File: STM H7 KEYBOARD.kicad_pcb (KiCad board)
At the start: 4 copper layers, 316.7 x 127 mm, 354 parts, among them J1 USB_C_Receptacle_USB2.0_16P, SW1 SW_Push, SW10 SW_Push, SW11 SW_Push, SW12 SW_Push, SW13 SW_Push, SW14 SW_Push, SW15 SW_Push, SW16 SW_Push, SW17 SW_Push, SW18 SW_Push, SW19 SW_Push, SW2 SW_Push, SW20 SW_Push, SW21 SW_Push, SW22 SW_Push, SW23 SW_Push, SW24 SW_Push, SW25 SW_Push, SW26 SW_Push, SW27 SW_Push, SW28 SW_Push, SW29 SW_Push, SW3 SW_Push, SW30 SW_Push, SW31 SW_Push, SW32 SW_Push, SW33 SW_Push, SW34 SW_Push, SW35 SW_Push, SW36 SW_Push, SW37 SW_Push, SW38 SW_Push, SW39 SW_Push, SW4 SW_Push, SW40 SW_Push, SW41 SW_Push, SW42 SW_Push, SW43 SW_Push, SW44 SW_Push, SW45 SW_Push, SW46 SW_Push, SW47 SW_Push, SW48 SW_Push, SW49 SW_Push, SW5 SW_Push, SW50 SW_Push, SW51 SW_Push, SW52 SW_Push, SW53 SW_Push, SW54 SW_Push, SW55 SW_Push, SW56 SW_Push, SW57 SW_Push, SW58 SW_Push, SW59 SW_Push, SW6 SW_Push, SW60 SW_Push, SW61 SW_Push, SW62 SW_Push, SW63 SW_Push, SW64 SW_Push, SW65 SW_Push, SW66 SW_Push, SW67 SW_Push, SW68 SW_Push, SW7 SW_Push, SW8 SW_Push, SW9 SW_Push, U1 USBLC6-2SC6, U2 AP63203WU, U4 STM32H723VGTx, U5 SN74AHCT1G125DBVR, U6 TPS25940LRVCR, U7 TUSB320LAIRWBR, Y1 8MHz

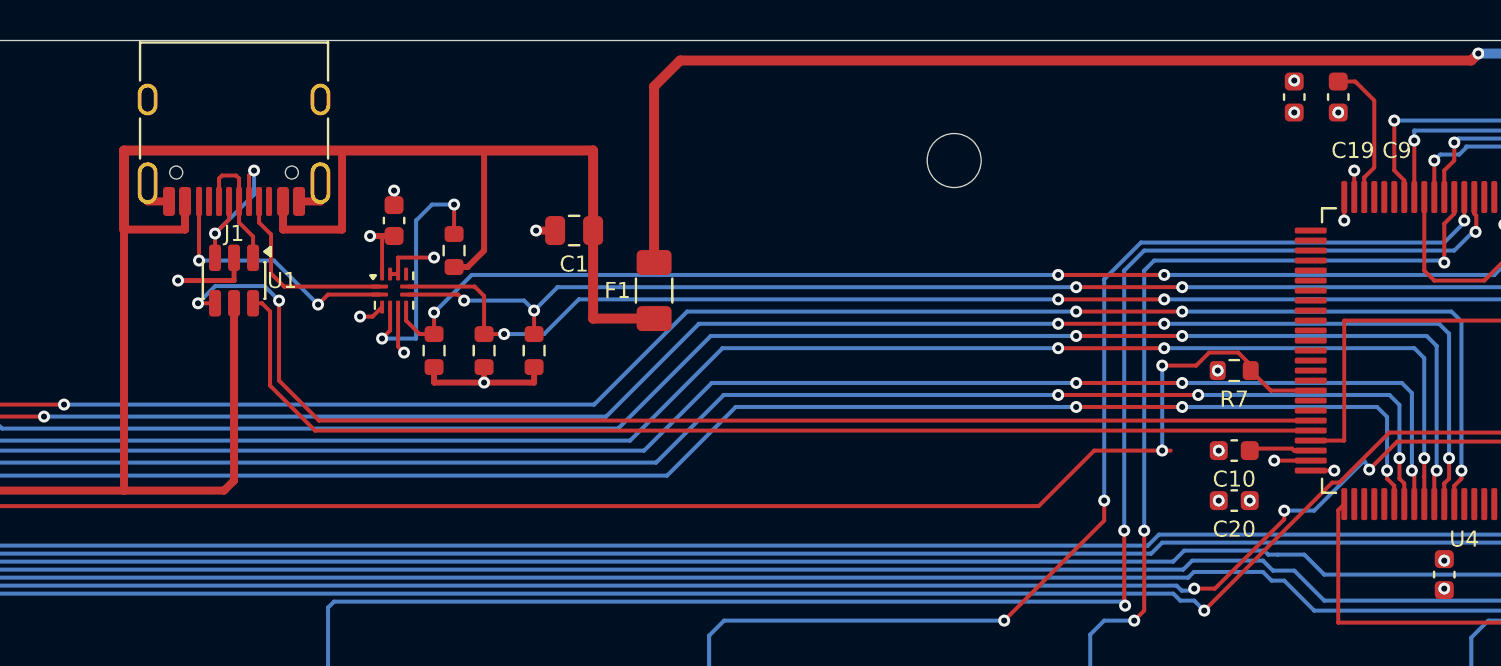
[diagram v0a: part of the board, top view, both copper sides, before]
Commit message: Fixed usb routing
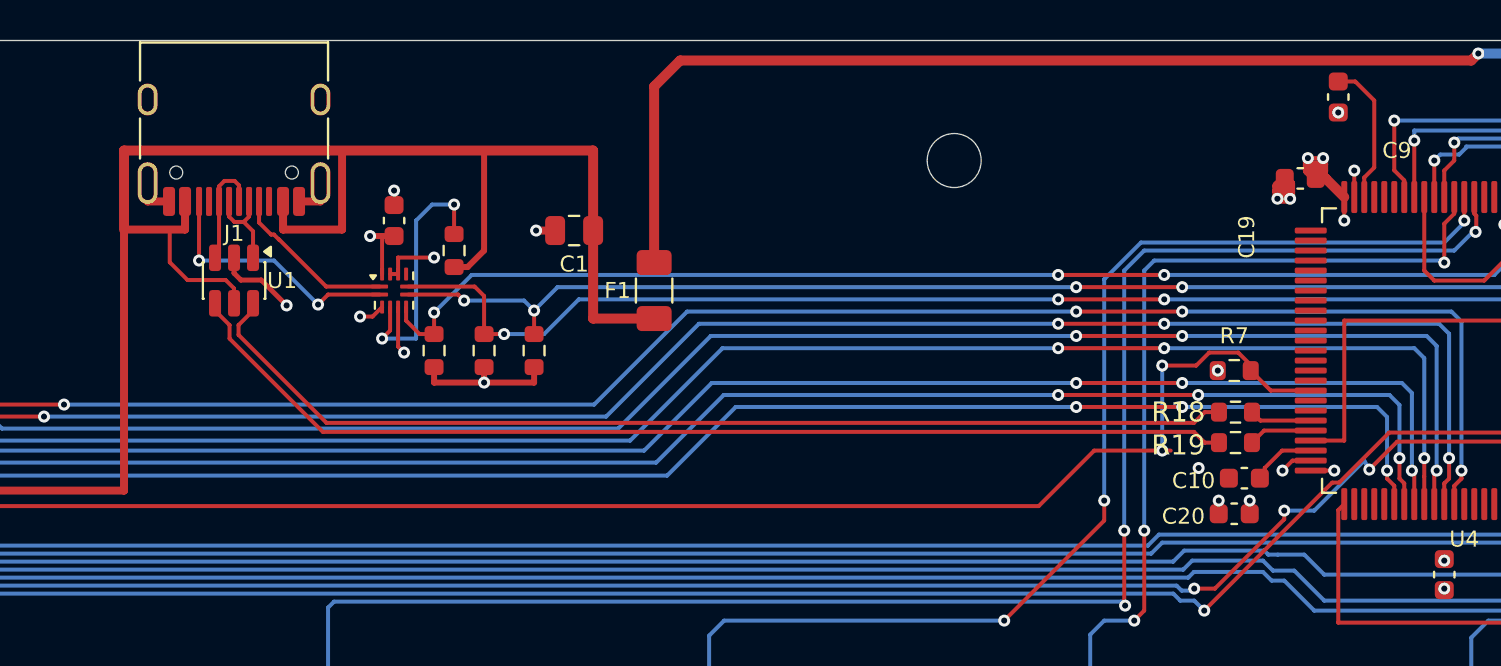
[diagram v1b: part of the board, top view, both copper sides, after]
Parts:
- added R18: 22, Resistor_SMD:R_0603_1608Metric, F.Cu at (246.1, 52.6)
- added R19: 22, Resistor_SMD:R_0603_1608Metric, F.Cu at (246.1, 54.1)
- R10: value 51.1k/0.1% -> 44.2k/0.1%
- moved C19 4.08 mm to (249.3, 40.9), turned to 180 degrees
- moved C10 1.47 mm to (246.5, 55.9)
- moved C20 0.66 mm to (246.0, 57.7)
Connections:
- U1 pad 1: USB_DP_PORT -> USB_DM_PORT
- U1 pad 3: USB_DM_PORT -> USB_DP_PORT
- U1 pad 4: USB_DM -> USB+
- U1 pad 6: USB_DP -> USB-
- U4 pad 70: USB_DM -> Net-(U4-PA11)
- U4 pad 71: USB_DP -> Net-(U4-PA12)
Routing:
- net USB_DM: track 62.0 -> 0.00 mm, vias 2 -> 0
- net USB_DP: track 57.7 -> 0.00 mm
- net USB+: track 0.00 -> 53.7 mm
- net USB-: track 0.00 -> 52.9 mm
- net VBUS_RAW: track 153.9 -> 145.5 mm
- net +3.3V: track 305.2 -> 310.9 mm, vias 29 -> 30
- net USB_DM_PORT: track 8.71 -> 4.72 mm, vias 2 -> 0
- net GND: track 63.8 -> 67.3 mm, vias 188 -> 189
- net Net-(U4-PA12): track 0.00 -> 3.19 mm
- net Net-(U4-PA11): track 0.00 -> 3.11 mm
- net USB_CC1: track 9.55 -> 8.41 mm
- net USB_DP_PORT: track 6.52 -> 5.66 mm
